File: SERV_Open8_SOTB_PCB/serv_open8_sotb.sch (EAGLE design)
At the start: 158 parts, among them IC1 TPS76201DBVR, IC12 SN74LVC1GU04DBVR, IC13 SN74LVC1GU04DBVR, IC2 TPS76201DBVR, IC5 TPS76201DBVR, IC7 TPS76201DBVR, IC8 TPS76201DBVR, IC9 TPS76201DBVR, Q1 BSH103,235, Q10 BSH103,235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

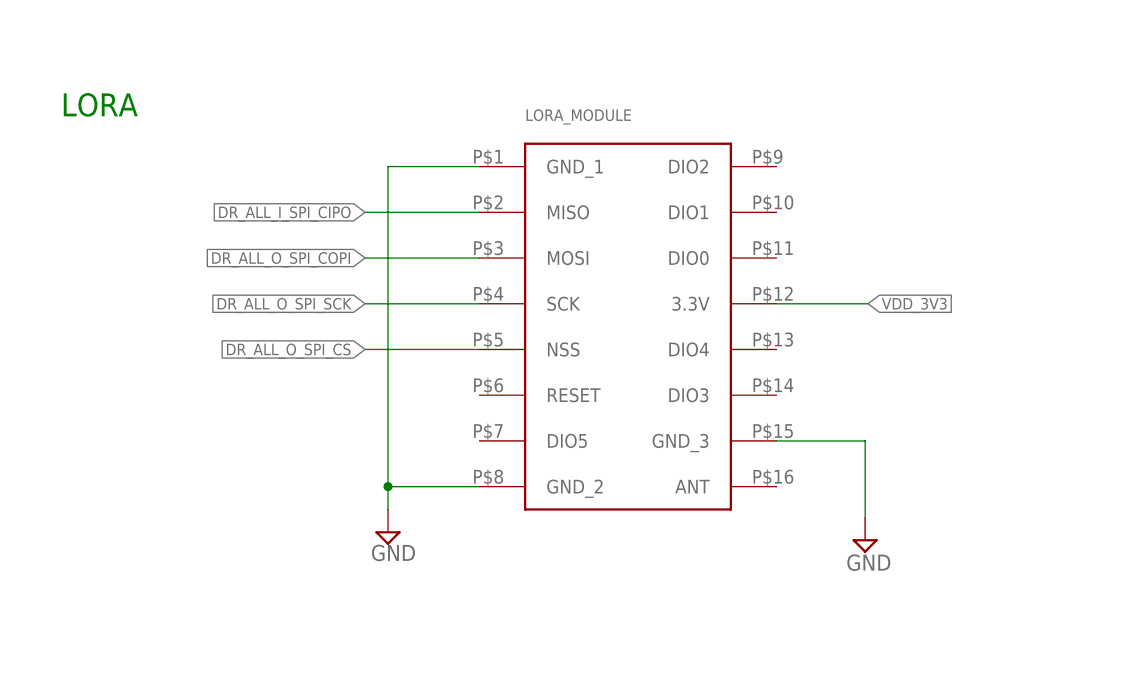
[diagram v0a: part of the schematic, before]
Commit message: Update new footprint for Lora module
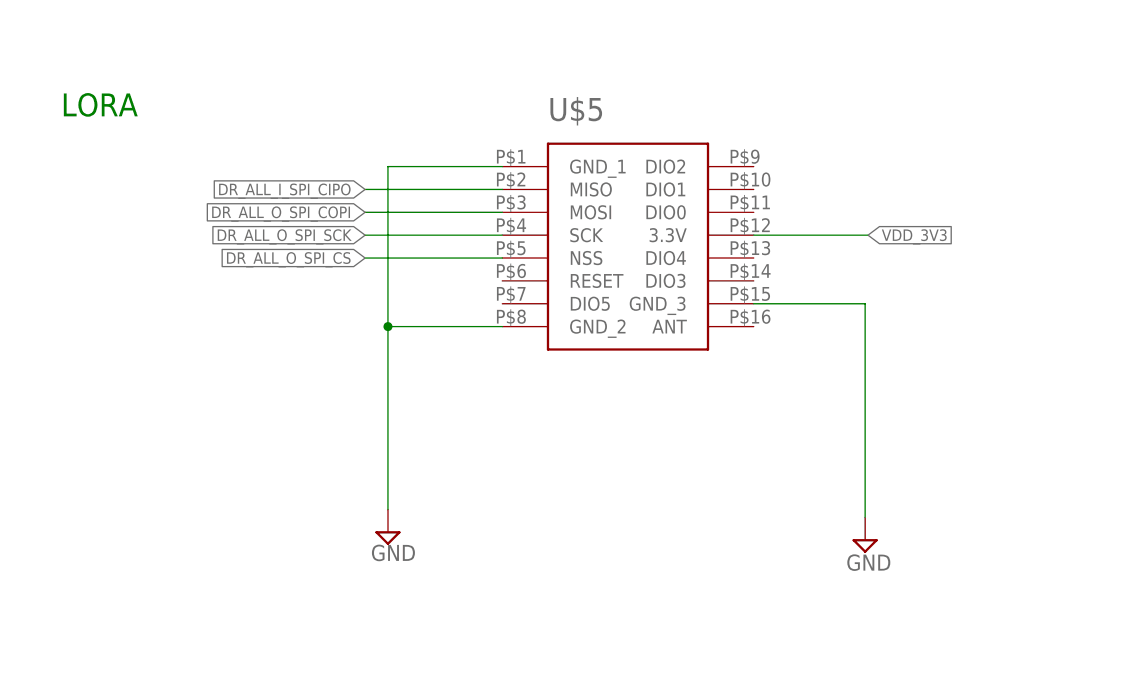
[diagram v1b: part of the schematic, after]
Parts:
- removed LORA_MODULE: (no value), qfp160:RFM95W-915S2
- added U$5: (no value), Duy:RFM95W-915S2
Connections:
- net DR_ALL_I_SPI_CIPO: now also U$5.MISO; no longer LORA_MODULE.MISO
- net DR_ALL_O_SPI_COPI: now also U$5.MOSI; no longer LORA_MODULE.MOSI
- net DR_ALL_O_SPI_CS: now also U$5.NSS; no longer LORA_MODULE.NSS
- net DR_ALL_O_SPI_SCK: now also U$5.SCK; no longer LORA_MODULE.SCK
- net GND: now also U$5.GND_1, U$5.GND_2, U$5.GND_3; no longer LORA_MODULE.GND_1, LORA_MODULE.GND_2, LORA_MODULE.GND_3
- net VDD_3V3: now also U$5.3.3V; no longer LORA_MODULE.3.3V
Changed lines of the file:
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@@
 <part name="U$4" library="Duy" deviceset="2X41_HEADER" device=""/>
 <part name="SUPPLY40" library="supply2" library_urn="urn:adsk.eagle:library:372" deviceset="GND" device=""/>
-<part name="LORA_MODULE" library="qfp160" deviceset="RFM95W-915S2" device=""/>
 <part name="SUPPLY58" library="supply2" library_urn="urn:adsk.eagle:library:372" deviceset="GND" device=""/>
 <part name="FLASH" library="Connector" library_urn="urn:adsk.eagle:library:16378166" deviceset="PINHD-2X6" device="" package3d_urn="urn:adsk.eagle:package:22474/2"/>
@@
 <part name="H4" library="holes" library_urn="urn:adsk.eagle:library:237" deviceset="MOUNT-HOLE" device="3.3" package3d_urn="urn:adsk.eagle:package:14278/1"/>
 <part name="FRAME1" library="frames" library_urn="urn:adsk.eagle:library:229" deviceset="FRAME_D_L" device=""/>
+<part name="U$5" library="Duy" deviceset="RFM95W-915S2" device=""/>
 </parts>
 <sheets>
@@
 <attribute name="VALUE" x="58.533" y="262.447" size="1.778" layer="96"/>
 </instance>
-<instance part="LORA_MODULE" gate="G$1" x="33.02" y="292.1" smashed="yes">
-<attribute name="NAME" x="22.86" y="312.42" size="1.27" layer="95"/>
-<attribute name="VALUE" x="25.4" y="266.7" size="1.27" layer="96"/>
-</instance>
 <instance part="SUPPLY58" gate="GND" x="7.62" y="266.7" smashed="yes">
 <attribute name="VALUE" x="5.715" y="263.525" size="1.778" layer="96"/>
@@
 <attribute name="DRAWING_NAME" x="373.38" y="-232.41" size="2.54" layer="94"/>
 </instance>
+<instance part="U$5" gate="G$1" x="33.02" y="299.72" smashed="yes">
+<attribute name="NAME" x="25.4" y="312.42" size="2.54" layer="95"/>
+<attribute name="VALUE" x="25.4" y="281.94" size="2.54" layer="96"/>
+</instance>
 </instances>
 <busses>
@@
 </segment>
 <segment>
-<pinref part="LORA_MODULE" gate="G$1" pin="GND_3"/>
 <pinref part="SUPPLY40" gate="GND" pin="GND"/>
-<wire x1="50.8" y1="276.86" x2="60.638" y2="276.86" width="0.1524" layer="91"/>
-<wire x1="60.638" y1="276.86" x2="60.638" y2="268.362" width="0.1524" layer="91"/>
-</segment>
-<segment>
-<pinref part="LORA_MODULE" gate="G$1" pin="GND_1"/>
-<wire x1="17.78" y1="307.34" x2="7.62" y2="307.34" width="0.1524" layer="91"/>
-<wire x1="7.62" y1="307.34" x2="7.62" y2="271.78" width="0.1524" layer="91"/>
+<wire x1="48.26" y1="292.1" x2="60.638" y2="292.1" width="0.1524" layer="91"/>
+<wire x1="60.638" y1="292.1" x2="60.638" y2="268.362" width="0.1524" layer="91"/>
+<pinref part="U$5" gate="G$1" pin="GND_3"/>
+</segment>
+<segment>
+<wire x1="20.32" y1="307.34" x2="7.62" y2="307.34" width="0.1524" layer="91"/>
+<wire x1="7.62" y1="307.34" x2="7.62" y2="289.56" width="0.1524" layer="91"/>
 <pinref part="SUPPLY58" gate="GND" pin="GND"/>
-<pinref part="LORA_MODULE" gate="G$1" pin="GND_2"/>
-<wire x1="7.62" y1="271.78" x2="7.62" y2="269.24" width="0.1524" layer="91"/>
-<wire x1="17.78" y1="271.78" x2="7.62" y2="271.78" width="0.1524" layer="91"/>
-<junction x="7.62" y="271.78"/>
+<wire x1="7.62" y1="289.56" x2="7.62" y2="269.24" width="0.1524" layer="91"/>
+<wire x1="20.32" y1="289.56" x2="7.62" y2="289.56" width="0.1524" layer="91"/>
+<junction x="7.62" y="289.56"/>
+<pinref part="U$5" gate="G$1" pin="GND_1"/>
+<pinref part="U$5" gate="G$1" pin="GND_2"/>
 </segment>
 <segment>
@@
 </segment>
 <segment>
-<pinref part="LORA_MODULE" gate="G$1" pin="3.3V"/>
-<wire x1="50.8" y1="292.1" x2="60.96" y2="292.1" width="0.1524" layer="91"/>
-<label x="60.96" y="292.1" size="1.27" layer="95" xref="yes"/>
+<wire x1="48.26" y1="299.72" x2="60.96" y2="299.72" width="0.1524" layer="91"/>
+<label x="60.96" y="299.72" size="1.27" layer="95" xref="yes"/>
+<pinref part="U$5" gate="G$1" pin="3.3V"/>
 </segment>
 <segment>
@@
 </segment>
 <segment>
-<pinref part="LORA_MODULE" gate="G$1" pin="SCK"/>
-<wire x1="17.78" y1="292.1" x2="5.08" y2="292.1" width="0.1524" layer="91"/>
-<label x="5.08" y="292.1" size="1.27" layer="95" rot="R180" xref="yes"/>
+<wire x1="20.32" y1="299.72" x2="5.08" y2="299.72" width="0.1524" layer="91"/>
+<label x="5.08" y="299.72" size="1.27" layer="95" rot="R180" xref="yes"/>
+<pinref part="U$5" gate="G$1" pin="SCK"/>
 </segment>
 </net>
@@
 </segment>
 <segment>
-<pinref part="LORA_MODULE" gate="G$1" pin="MOSI"/>
-<wire x1="17.78" y1="297.18" x2="5.08" y2="297.18" width="0.1524" layer="91"/>
-<label x="5.08" y="297.18" size="1.27" layer="95" rot="R180" xref="yes"/>
+<wire x1="20.32" y1="302.26" x2="5.08" y2="302.26" width="0.1524" layer="91"/>
+<label x="5.08" y="302.26" size="1.27" layer="95" rot="R180" xref="yes"/>
+<pinref part="U$5" gate="G$1" pin="MOSI"/>
 </segment>
 </net>
@@
 </segment>
 <segment>
-<pinref part="LORA_MODULE" gate="G$1" pin="MISO"/>
-<wire x1="17.78" y1="302.26" x2="5.08" y2="302.26" width="0.1524" layer="91"/>
-<label x="5.08" y="302.26" size="1.27" layer="95" rot="R180" xref="yes"/>
+<wire x1="20.32" y1="304.8" x2="5.08" y2="304.8" width="0.1524" layer="91"/>
+<label x="5.08" y="304.8" size="1.27" layer="95" rot="R180" xref="yes"/>
+<pinref part="U$5" gate="G$1" pin="MISO"/>
 </segment>
 </net>
@@
 </segment>
 <segment>
-<pinref part="LORA_MODULE" gate="G$1" pin="NSS"/>
-<wire x1="17.78" y1="287.02" x2="5.08" y2="287.02" width="0.1524" layer="91"/>
-<label x="5.08" y="287.02" size="1.27" layer="95" rot="R180" xref="yes"/>
-</segment>
-</net>
+<wire x1="20.32" y1="297.18" x2="5.08" y2="297.18" width="0.1524" layer="91"/>
+<label x="5.08" y="297.18" size="1.27" layer="95" rot="R180" xref="yes"/>
+<pinref part="U$5" gate="G$1" pin="NSS"/>
+</segment>
+</net>

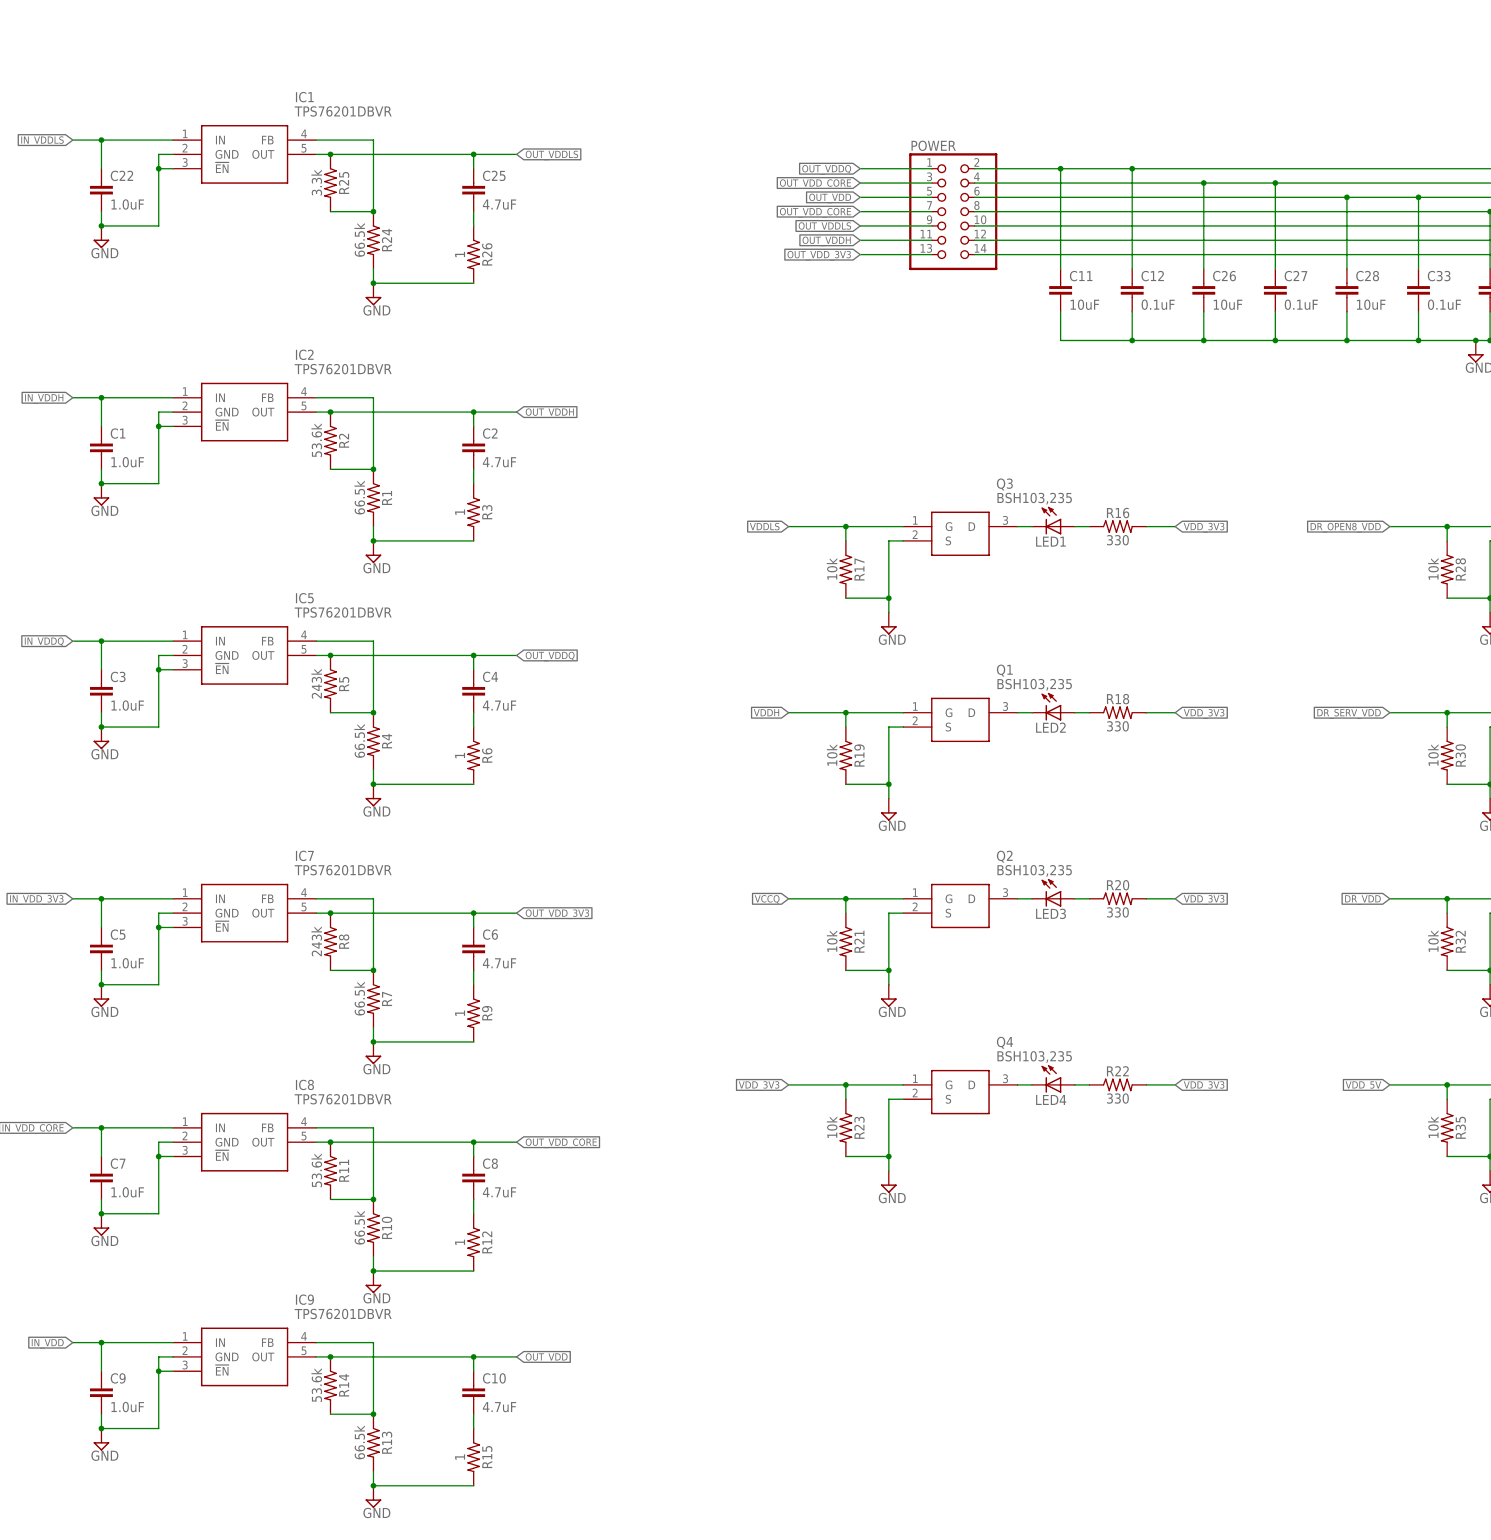
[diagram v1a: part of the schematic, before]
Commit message: Update new regulators
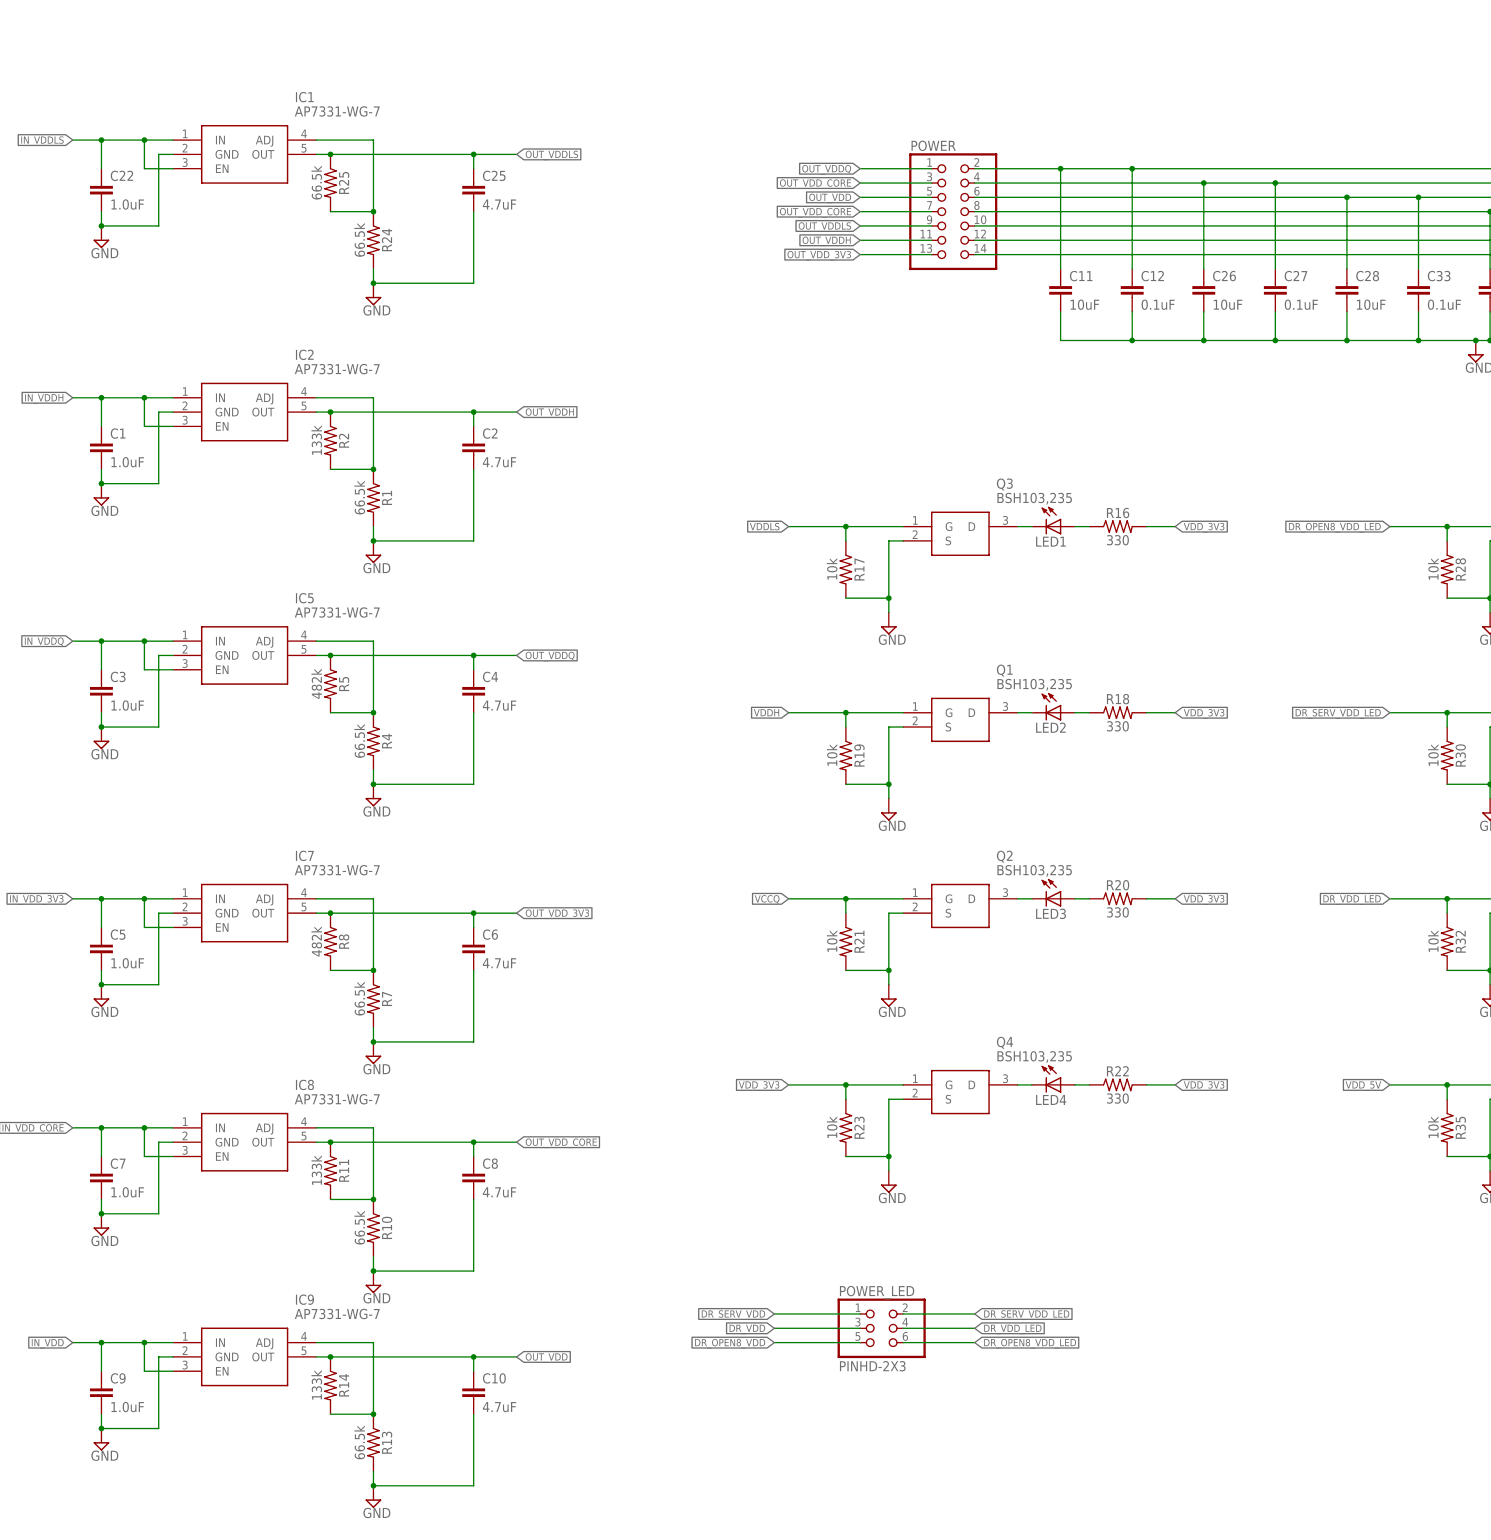
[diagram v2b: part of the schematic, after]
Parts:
- removed R12, R15, R26, R3, R6, R9: 1, SparkFun-Resistors:0.3OHM-0805-1/8W-1%
- added POWER_LED: PINHD-2X3, Connector:PINHD-2X3
- IC1, IC2, IC5, IC7, IC8, IC9: value TPS76201DBVR -> AP7331-WG-7; device SamacSys_Parts:TPS76201DBVR -> SamacSys_Parts:AP7331-WG-7
- R11, R14, R2: value 53.6k -> 133k
- R25: value 3.3k -> 66.5k
- R5, R8: value 243k -> 482k
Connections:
- removed net N$12: C10.2, R15.1
- removed net N$19: C25.2, R26.1
- removed net N$2: C2.2, R3.1
- removed net N$4: C4.2, R6.1
- removed net N$6: C6.2, R9.1
- removed net N$8: C8.2, R12.1
- new net DR_OPEN8_VDD_LED: POWER_LED.6, Q5.G, R28.1
- new net DR_SERV_VDD_LED: POWER_LED.2, Q6.G, R30.1
- new net DR_VDD_LED: POWER_LED.4, Q7.G, R32.1
- net DR_OPEN8_VDD: now also POWER_LED.5; no longer Q5.G, R28.1
- net DR_SERV_VDD: now also POWER_LED.1; no longer Q6.G, R30.1
- net DR_VDD: now also POWER_LED.3; no longer Q7.G, R32.1
- net GND: now also C10.2, C2.2, C25.2, C4.2, C6.2, C8.2; no longer IC1.!EN, IC2.!EN, IC5.!EN, IC7.!EN, IC8.!EN, IC9.!EN, R12.2, R15.2, R26.2, R3.2, R6.2, R9.2
- net IN_VDD: now also IC9.EN
- net IN_VDDH: now also IC2.EN
- net IN_VDDLS: now also IC1.EN
- net IN_VDDQ: now also IC5.EN
- net IN_VDD_3V3: now also IC7.EN
- net IN_VDD_CORE: now also IC8.EN
- net N$1: now also IC2.ADJ; no longer IC2.FB
- net N$18: now also IC1.ADJ; no longer IC1.FB
- net N$3: now also IC5.ADJ; no longer IC5.FB
- net N$5: now also IC7.ADJ; no longer IC7.FB
- net N$7: now also IC8.ADJ; no longer IC8.FB
- net N$9: now also IC9.ADJ; no longer IC9.FB
